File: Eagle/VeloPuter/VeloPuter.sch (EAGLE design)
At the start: 36 parts, among them IC1 LM2931Z

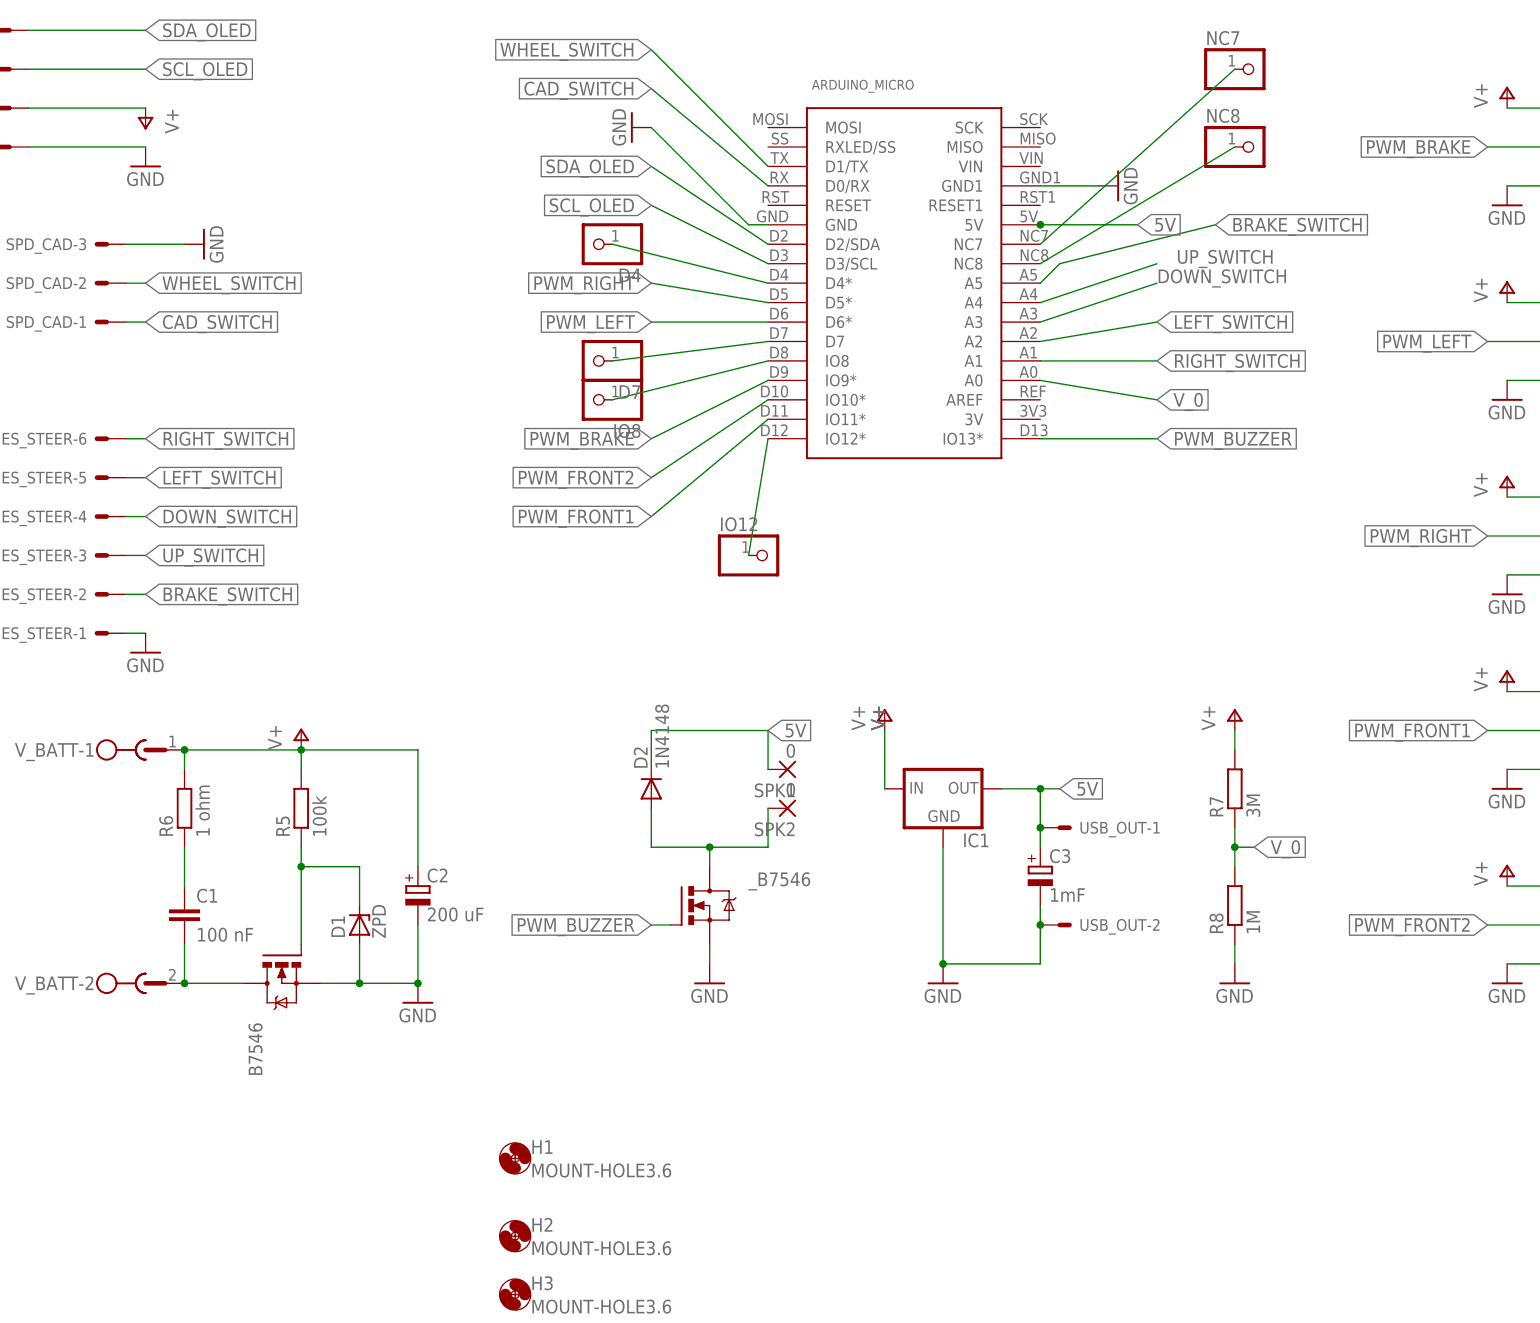
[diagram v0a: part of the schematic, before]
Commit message: Partial redesign due to insights from the first builds - VDD of the oled now goes to the 5V not Vbatt. - Larger capacitor for C2. - LM2931 replaced by a TO220 (need new layout for this) - Brake handle now goes to pin nr 7 because that is a pin with an interupt. - reorganised the free pins. - Allowed for some wirering below the arduinio itself (for now just the extra pins which are used) -
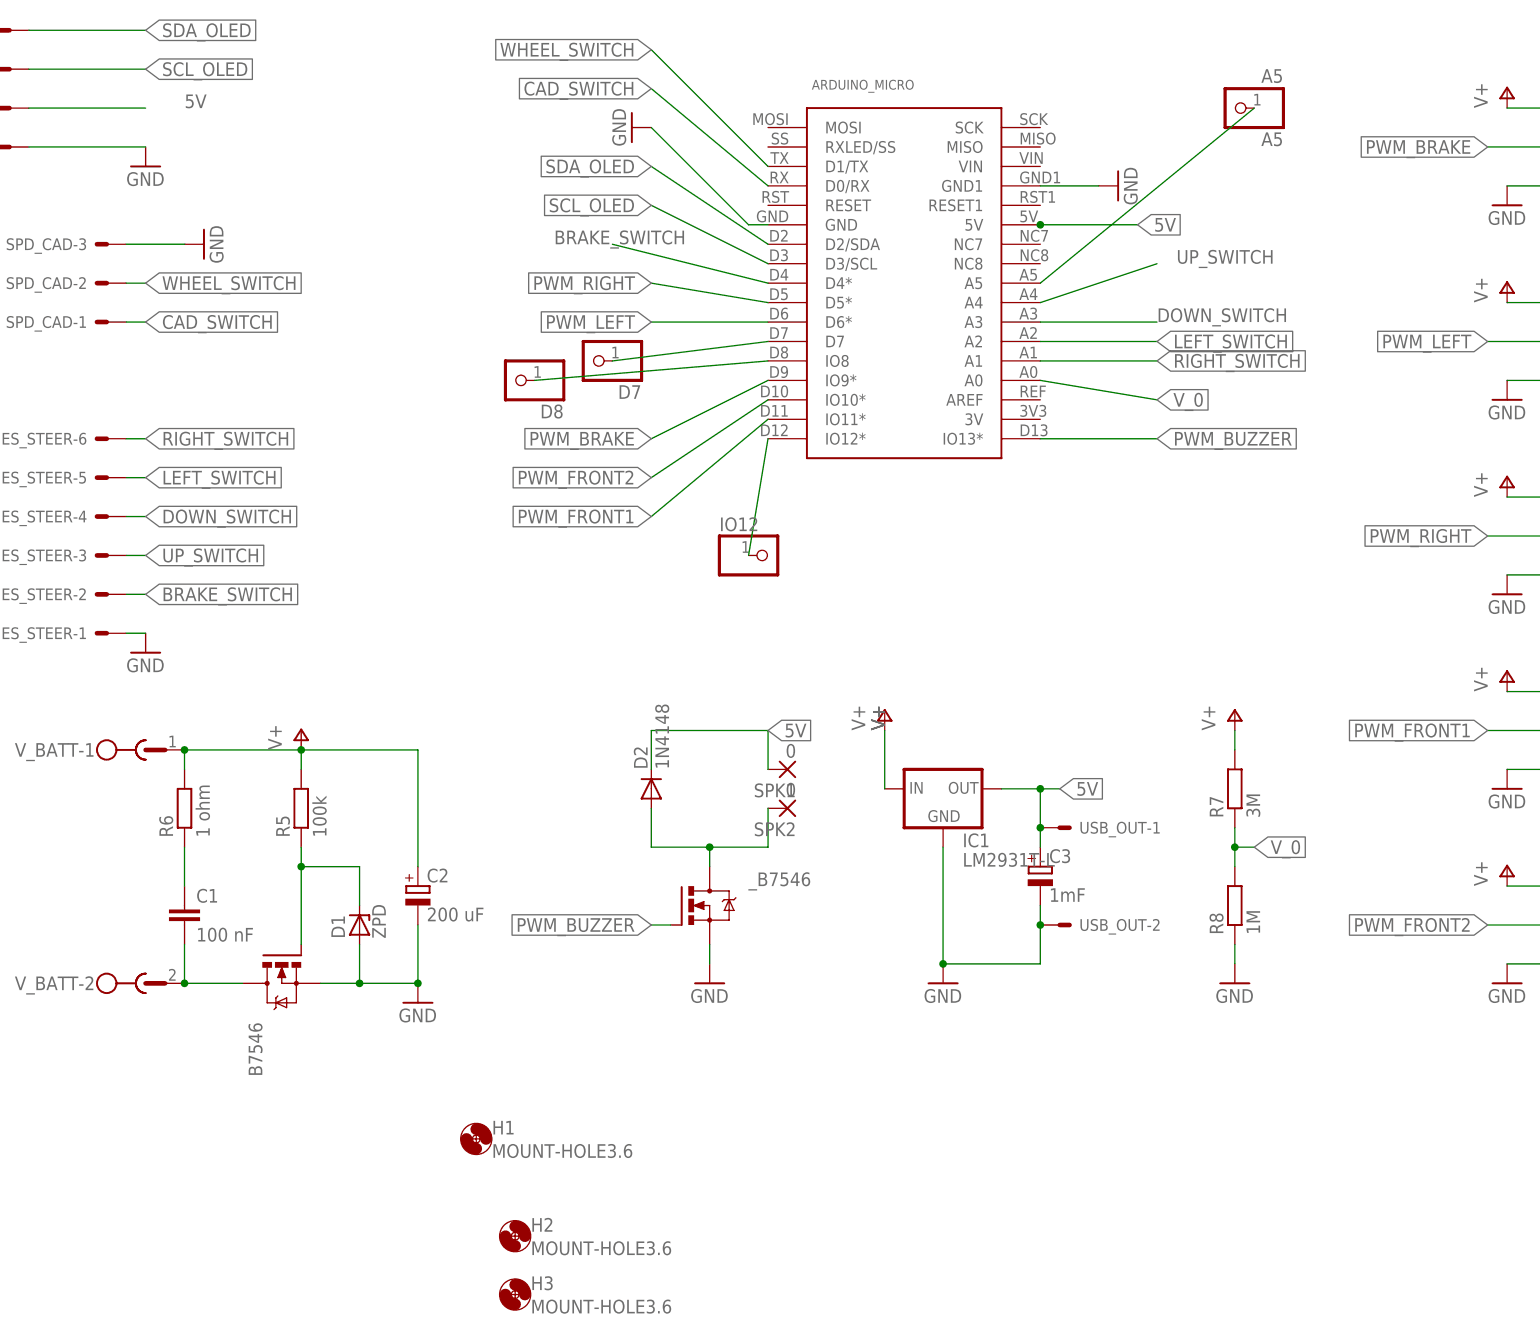
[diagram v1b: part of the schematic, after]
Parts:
- removed D4, IO8, NC7, NC8: (no value), pinhead:PINHD-1X1
- added A5: A5, pinhead:PINHD-1X1
- added D8: (no value), pinhead:PINHD-1X1
- C2: device rcl:CPOL-EUE2.5-7 -> rcl:CPOL-EUE5-10.5
- IC1: value LM2931Z -> LM2931T-L; device v-reg-3:LM2931Z -> v-reg-3:LM2931T-L
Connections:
- removed net N$15: ARDUINO_MICRO.D4*, D4.1
- removed net N$19: ARDUINO_MICRO.NC8, NC8.1
- removed net N$20: ARDUINO_MICRO.NC7, NC7.1
- new net A5: A5.1, ARDUINO_MICRO.A5
- net 5V: now also OLED-3.S
- net BRAKE_SWITCH: now also ARDUINO_MICRO.D4*; no longer ARDUINO_MICRO.A5
- net N$17: now also D8.1; no longer IO8.1
- net V+: no longer OLED-3.S
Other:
- moved on the sheet: H1
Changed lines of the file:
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@@
 <part name="GND7" library="supply1" deviceset="GND" device=""/>
 <part name="GND8" library="supply1" deviceset="GND" device=""/>
-<part name="P+7" library="supply1" deviceset="V+" device=""/>
 <part name="SWITCHES_STEER" library="con-molex" deviceset="22-?-06" device="27-2061" value=""/>
 <part name="SPD_CAD" library="con-molex" deviceset="22-?-03" device="27-2031" value=""/>
@@
 </part>
 <part name="P+1" library="supply1" deviceset="V+" device=""/>
-<part name="C2" library="rcl" deviceset="CPOL-EU" device="E2.5-7" value="200 uF">
-<attribute name="MF" value=""/>
-<attribute name="MPN" value=""/>
-<attribute name="OC_NEWARK" value="unknown"/>
-</part>
-<part name="IC1" library="v-reg-3" deviceset="LM2931" device="Z" value="">
+<part name="C2" library="rcl" deviceset="CPOL-EU" device="E5-10.5" value="200 uF">
+<attribute name="MF" value=""/>
+<attribute name="MPN" value=""/>
+<attribute name="OC_NEWARK" value="unknown"/>
+</part>
+<part name="IC1" library="v-reg-3" deviceset="LM2931" device="T-L" value="LM2931T-L">
 <attribute name="MF" value=""/>
 <attribute name="MPN" value=""/>
@@
 <attribute name="OC_NEWARK" value="unknown"/>
 </part>
-<part name="IO8" library="pinhead" deviceset="PINHD-1X1" device="">
+<part name="D8" library="pinhead" deviceset="PINHD-1X1" device="">
 <attribute name="MF" value=""/>
 <attribute name="MPN" value=""/>
@@
 <attribute name="OC_NEWARK" value="unknown"/>
 </part>
-<part name="D4" library="pinhead" deviceset="PINHD-1X1" device="">
-<attribute name="MF" value=""/>
-<attribute name="MPN" value=""/>
-<attribute name="OC_NEWARK" value="unknown"/>
-</part>
-<part name="NC7" library="pinhead" deviceset="PINHD-1X1" device="">
-<attribute name="MF" value=""/>
-<attribute name="MPN" value=""/>
-<attribute name="OC_NEWARK" value="unknown"/>
-</part>
-<part name="NC8" library="pinhead" deviceset="PINHD-1X1" device="">
+<part name="A5" library="pinhead" deviceset="PINHD-1X1" device="" value="A5">
 <attribute name="MF" value=""/>
 <attribute name="MPN" value=""/>
@@
 <instance part="GND7" gate="1" x="187.96" y="104.14"/>
 <instance part="GND8" gate="1" x="10.16" y="109.22"/>
-<instance part="P+7" gate="1" x="10.16" y="114.3" rot="R180"/>
 <instance part="SWITCHES_STEER" gate="-1" x="5.08" y="48.26" rot="R180"/>
 <instance part="SWITCHES_STEER" gate="-2" x="5.08" y="53.34" rot="R180"/>
@@
 <instance part="LIGHTS" gate="-5" x="236.22" y="116.84" rot="R180"/>
 <instance part="LIGHTS" gate="-6" x="236.22" y="106.68" rot="R180"/>
-<instance part="H1" gate="G$1" x="58.42" y="-20.32">
-<attribute name="OC_NEWARK" x="58.42" y="-20.32" size="1.778" layer="96" display="off"/>
-<attribute name="MF" x="58.42" y="-20.32" size="1.778" layer="96" display="off"/>
-<attribute name="MPN" x="58.42" y="-20.32" size="1.778" layer="96" display="off"/>
+<instance part="H1" gate="G$1" x="53.34" y="-17.78">
+<attribute name="OC_NEWARK" x="53.34" y="-17.78" size="1.778" layer="96" display="off"/>
+<attribute name="MF" x="53.34" y="-17.78" size="1.778" layer="96" display="off"/>
+<attribute name="MPN" x="53.34" y="-17.78" size="1.778" layer="96" display="off"/>
 </instance>
 <instance part="H2" gate="G$1" x="58.42" y="-30.48">
@@
 <attribute name="MPN" x="58.42" y="-38.1" size="1.778" layer="96" display="off"/>
 </instance>
-<instance part="IO8" gate="G$1" x="68.58" y="78.74" rot="R180">
-<attribute name="OC_NEWARK" x="68.58" y="78.74" size="1.778" layer="96" display="off"/>
-<attribute name="MF" x="68.58" y="78.74" size="1.778" layer="96" display="off"/>
-<attribute name="MPN" x="68.58" y="78.74" size="1.778" layer="96" display="off"/>
+<instance part="D8" gate="G$1" x="58.42" y="81.28" rot="R180">
+<attribute name="OC_NEWARK" x="58.42" y="81.28" size="1.778" layer="96" display="off"/>
+<attribute name="MF" x="58.42" y="81.28" size="1.778" layer="96" display="off"/>
+<attribute name="MPN" x="58.42" y="81.28" size="1.778" layer="96" display="off"/>
 </instance>
 <instance part="IO12" gate="G$1" x="91.44" y="58.42">
@@
 <attribute name="MPN" x="91.44" y="58.42" size="1.778" layer="96" display="off"/>
 </instance>
-<instance part="D4" gate="G$1" x="68.58" y="99.06" rot="R180">
-<attribute name="OC_NEWARK" x="68.58" y="99.06" size="1.778" layer="96" display="off"/>
-<attribute name="MF" x="68.58" y="99.06" size="1.778" layer="96" display="off"/>
-<attribute name="MPN" x="68.58" y="99.06" size="1.778" layer="96" display="off"/>
-</instance>
-<instance part="NC7" gate="G$1" x="154.94" y="121.92">
-<attribute name="OC_NEWARK" x="154.94" y="121.92" size="1.778" layer="96" display="off"/>
-<attribute name="MF" x="154.94" y="121.92" size="1.778" layer="96" display="off"/>
-<attribute name="MPN" x="154.94" y="121.92" size="1.778" layer="96" display="off"/>
-</instance>
-<instance part="NC8" gate="G$1" x="154.94" y="111.76">
-<attribute name="OC_NEWARK" x="154.94" y="111.76" size="1.778" layer="96" display="off"/>
-<attribute name="MF" x="154.94" y="111.76" size="1.778" layer="96" display="off"/>
-<attribute name="MPN" x="154.94" y="111.76" size="1.778" layer="96" display="off"/>
+<instance part="A5" gate="G$1" x="152.4" y="116.84" rot="R180">
+<attribute name="OC_NEWARK" x="152.4" y="116.84" size="1.778" layer="96" display="off"/>
+<attribute name="MF" x="152.4" y="116.84" size="1.778" layer="96" display="off"/>
+<attribute name="MPN" x="152.4" y="116.84" size="1.778" layer="96" display="off"/>
 </instance>
 <instance part="D7" gate="G$1" x="68.58" y="83.82" rot="R180">
@@
 <pinref part="U$5" gate="G$1" pin="DCIN+"/>
 <wire x1="187.96" y1="15.24" x2="195.58" y2="15.24" width="0.1524" layer="91"/>
-</segment>
-<segment>
-<pinref part="P+7" gate="1" pin="V+"/>
-<pinref part="OLED" gate="-3" pin="S"/>
-<wire x1="-5.08" y1="116.84" x2="10.16" y2="116.84" width="0.1524" layer="91"/>
 </segment>
 <segment>
@@
 <segment>
 <pinref part="ARDUINO_MICRO" gate="G$1" pin="A3"/>
-<wire x1="127" y1="88.9" x2="142.24" y2="93.98" width="0.1524" layer="91"/>
-<label x="142.24" y="93.98" size="1.778" layer="95"/>
+<wire x1="127" y1="88.9" x2="142.24" y2="88.9" width="0.1524" layer="91"/>
+<label x="142.24" y="88.9" size="1.778" layer="95"/>
 </segment>
 <segment>
@@
 <segment>
 <pinref part="ARDUINO_MICRO" gate="G$1" pin="A2"/>
-<wire x1="127" y1="86.36" x2="142.24" y2="88.9" width="0.1524" layer="91"/>
-<label x="142.24" y="88.9" size="1.778" layer="95" xref="yes"/>
+<wire x1="127" y1="86.36" x2="142.24" y2="86.36" width="0.1524" layer="91"/>
+<label x="142.24" y="86.36" size="1.778" layer="95" xref="yes"/>
 </segment>
 <segment>
@@
 <net name="BRAKE_SWITCH" class="0">
 <segment>
-<label x="149.86" y="101.6" size="1.778" layer="95" xref="yes"/>
-<pinref part="ARDUINO_MICRO" gate="G$1" pin="A5"/>
-<wire x1="149.86" y1="101.6" x2="129.54" y2="96.52" width="0.1524" layer="91"/>
-<wire x1="129.54" y1="96.52" x2="127" y2="93.98" width="0.1524" layer="91"/>
-</segment>
-<segment>
 <pinref part="SWITCHES_STEER" gate="-2" pin="S"/>
 <wire x1="7.62" y1="53.34" x2="10.16" y2="53.34" width="0.1524" layer="91"/>
 <label x="10.16" y="53.34" size="1.778" layer="95" xref="yes"/>
+</segment>
+<segment>
+<pinref part="ARDUINO_MICRO" gate="G$1" pin="D4*"/>
+<wire x1="71.12" y1="99.06" x2="91.44" y2="93.98" width="0.1524" layer="91"/>
+<label x="63.5" y="99.06" size="1.778" layer="95"/>
 </segment>
 </net>
@@
 <label x="91.44" y="35.56" size="1.778" layer="95" xref="yes"/>
 </segment>
+<segment>
+<pinref part="OLED" gate="-3" pin="S"/>
+<wire x1="-5.08" y1="116.84" x2="10.16" y2="116.84" width="0.1524" layer="91"/>
+<label x="15.24" y="116.84" size="1.778" layer="95"/>
+</segment>
 </net>
 <net name="N$4" class="0">
@@
 </segment>
 </net>
-<net name="N$15" class="0">
-<segment>
-<pinref part="ARDUINO_MICRO" gate="G$1" pin="D4*"/>
-<pinref part="D4" gate="G$1" pin="1"/>
-<wire x1="71.12" y1="99.06" x2="91.44" y2="93.98" width="0.1524" layer="91"/>
-</segment>
-</net>
 <net name="N$16" class="0">
 <segment>
@@
 <net name="N$17" class="0">
 <segment>
-<pinref part="IO8" gate="G$1" pin="1"/>
+<pinref part="D8" gate="G$1" pin="1"/>
 <pinref part="ARDUINO_MICRO" gate="G$1" pin="IO8"/>
-<wire x1="71.12" y1="78.74" x2="91.44" y2="83.82" width="0.1524" layer="91"/>
+<wire x1="60.96" y1="81.28" x2="91.44" y2="83.82" width="0.1524" layer="91"/>
 </segment>
 </net>
@@
 </segment>
 </net>
-<net name="N$19" class="0">
-<segment>
-<pinref part="NC8" gate="G$1" pin="1"/>
-<pinref part="ARDUINO_MICRO" gate="G$1" pin="NC8"/>
-<wire x1="152.4" y1="111.76" x2="127" y2="96.52" width="0.1524" layer="91"/>
-</segment>
-</net>
-<net name="N$20" class="0">
-<segment>
-<pinref part="NC7" gate="G$1" pin="1"/>
-<pinref part="ARDUINO_MICRO" gate="G$1" pin="NC7"/>
-<wire x1="152.4" y1="121.92" x2="127" y2="99.06" width="0.1524" layer="91"/>
-</segment>
-</net>
+<net name="A5" class="0">
+<segment>
+<pinref part="A5" gate="G$1" pin="1"/>
+<pinref part="ARDUINO_MICRO" gate="G$1" pin="A5"/>
+<wire x1="154.94" y1="116.84" x2="127" y2="93.98" width="0.1524" layer="91"/>
+</segment>
+</net>
